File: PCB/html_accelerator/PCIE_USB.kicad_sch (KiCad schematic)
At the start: 19 parts, among them U1 MCS9990, U2 AP1513

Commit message: cap updates
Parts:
- C33: footprint Capacitor_SMD:C_0805_2012Metric_Pad1.18x1.45mm_HandSolder -> Capacitor_SMD:CP_Elec_10x10
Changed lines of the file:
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@@
       (effects (font (size 1.27 1.27)) (justify left))
     )
-    (property "Footprint" "Capacitor_SMD:C_0805_2012Metric_Pad1.18x1.45mm_HandSolder" (at 44.45 154.94 0)
+    (property "Footprint" "Capacitor_SMD:CP_Elec_10x10" (at 44.45 154.94 0)
       (effects (font (size 1.27 1.27)) hide)
     )
@@
       (effects (font (size 1.27 1.27)) (justify left))
     )
-    (property "Footprint" "Capacitor_SMD:C_0805_2012Metric_Pad1.18x1.45mm_HandSolder" (at 148.59 154.94 0)
-      (effects (font (size 1.27 1.27)) hide)
-    )
+    (property "Footprint" "Capacitor_SMD:CP_Elec_10x10" (at 148.59 154.94 0)
+      (effects (font (size 1.27 1.27)) hide)
+    )

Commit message: placement updates
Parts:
- added C33 (x2): 100uF, Capacitor_SMD:CP_Elec_6.3x5.8, symbol Device:C_Polarized_US
- C33: value 470uF -> 100uF; footprint Capacitor_SMD:CP_Elec_10x10 -> Capacitor_SMD:CP_Elec_6.3x5.8
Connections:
- net +12V: now also C33.1
- net GND: now also C33.2, C33.2
- net +3V3 renamed +5V
- net +5V: now also C33.1

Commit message: layout and 3d updates
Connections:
- net USB0_DM renamed 90_USB0_D_N
- net USB0_DP renamed 90_USB0_D_P
- net USB1_DM renamed 90_USB1_D_N
- net USB1_DP renamed 90_USB1_D_P
- net USB2_DM renamed 90_USB2_D_N
- net USB2_DP renamed 90_USB2_D_P
- net USB3_DM renamed 90_USB3_D_N
- net USB3_DP renamed 90_USB3_D_P
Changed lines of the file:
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@@
     (effects (font (size 1.27 1.27)) (justify left bottom))
   )
-  (global_label "USB1_DM" (shape bidirectional) (at 147.32 58.42 0) (fields_autoplaced)
+  (global_label "90_USB1_D_N" (shape bidirectional) (at 147.32 58.42 0) (fields_autoplaced)
     (effects (font (size 1.27 1.27)) (justify left))
-    (property "Intersheetrefs" "${INTERSHEET_REFS}" (at 160.0456 58.42 0)
+    (property "Intersheetrefs" "${INTERSHEET_REFS}" (at 164.2789 58.42 0)
       (effects (font (size 1.27 1.27)) (justify left))
     )
   )
-  (global_label "USB0_DM" (shape bidirectional) (at 147.32 43.18 0) (fields_autoplaced)
+  (global_label "90_USB0_D_N" (shape bidirectional) (at 147.32 43.18 0) (fields_autoplaced)
     (effects (font (size 1.27 1.27)) (justify left))
-    (property "Intersheetrefs" "${INTERSHEET_REFS}" (at 160.0456 43.18 0)
+    (property "Intersheetrefs" "${INTERSHEET_REFS}" (at 164.2789 43.18 0)
       (effects (font (size 1.27 1.27)) (justify left))
     )
   )
-  (global_label "USB3_DM" (shape bidirectional) (at 147.32 88.9 0) (fields_autoplaced)
+  (global_label "90_USB3_D_N" (shape bidirectional) (at 147.32 88.9 0) (fields_autoplaced)
     (effects (font (size 1.27 1.27)) (justify left))
-    (property "Intersheetrefs" "${INTERSHEET_REFS}" (at 160.0456 88.9 0)
+    (property "Intersheetrefs" "${INTERSHEET_REFS}" (at 164.2789 88.9 0)
       (effects (font (size 1.27 1.27)) (justify left))
     )
   )
-  (global_label "USB2_DM" (shape bidirectional) (at 147.32 73.66 0) (fields_autoplaced)
+  (global_label "90_USB2_D_N" (shape bidirectional) (at 147.32 73.66 0) (fields_autoplaced)
     (effects (font (size 1.27 1.27)) (justify left))
-    (property "Intersheetrefs" "${INTERSHEET_REFS}" (at 160.0456 73.66 0)
+    (property "Intersheetrefs" "${INTERSHEET_REFS}" (at 164.2789 73.66 0)
       (effects (font (size 1.27 1.27)) (justify left))
     )
   )
-  (global_label "USB3_DP" (shape bidirectional) (at 147.32 93.98 0) (fields_autoplaced)
+  (global_label "90_USB3_D_P" (shape bidirectional) (at 147.32 93.98 0) (fields_autoplaced)
     (effects (font (size 1.27 1.27)) (justify left))
-    (property "Intersheetrefs" "${INTERSHEET_REFS}" (at 159.8642 93.98 0)
+    (property "Intersheetrefs" "${INTERSHEET_REFS}" (at 164.2184 93.98 0)
       (effects (font (size 1.27 1.27)) (justify left))
     )
   )
-  (global_label "USB2_DP" (shape bidirectional) (at 147.32 78.74 0) (fields_autoplaced)
+  (global_label "90_USB2_D_P" (shape bidirectional) (at 147.32 78.74 0) (fields_autoplaced)
     (effects (font (size 1.27 1.27)) (justify left))
-    (property "Intersheetrefs" "${INTERSHEET_REFS}" (at 159.8642 78.74 0)
+    (property "Intersheetrefs" "${INTERSHEET_REFS}" (at 164.2184 78.74 0)
       (effects (font (size 1.27 1.27)) (justify left))
     )
   )
-  (global_label "USB0_DP" (shape bidirectional) (at 147.32 48.26 0) (fields_autoplaced)
+  (global_label "90_USB0_D_P" (shape bidirectional) (at 147.32 48.26 0) (fields_autoplaced)
     (effects (font (size 1.27 1.27)) (justify left))
-    (property "Intersheetrefs" "${INTERSHEET_REFS}" (at 159.8642 48.26 0)
+    (property "Intersheetrefs" "${INTERSHEET_REFS}" (at 164.2184 48.26 0)
       (effects (font (size 1.27 1.27)) (justify left))
     )
   )
-  (global_label "USB1_DP" (shape bidirectional) (at 147.32 63.5 0) (fields_autoplaced)
+  (global_label "90_USB1_D_P" (shape bidirectional) (at 147.32 63.5 0) (fields_autoplaced)
     (effects (font (size 1.27 1.27)) (justify left))
-    (property "Intersheetrefs" "${INTERSHEET_REFS}" (at 159.8642 63.5 0)
+    (property "Intersheetrefs" "${INTERSHEET_REFS}" (at 164.2184 63.5 0)
       (effects (font (size 1.27 1.27)) (justify left))
     )

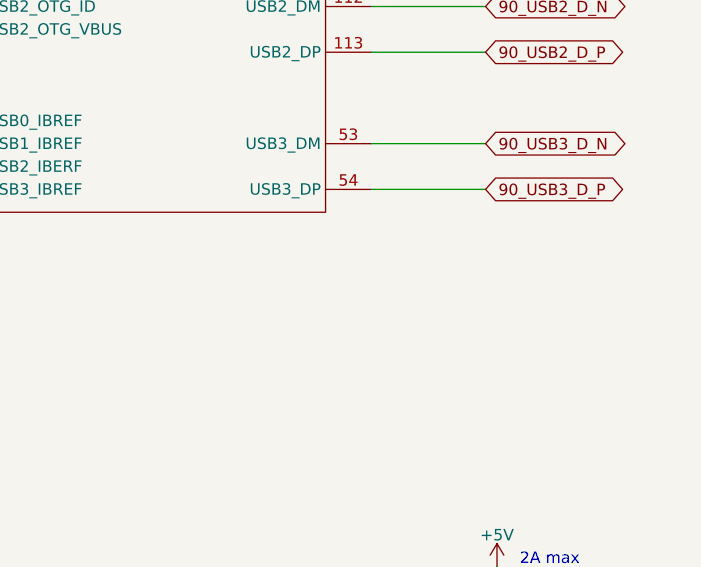
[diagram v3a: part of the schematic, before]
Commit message: impedance controlled nets
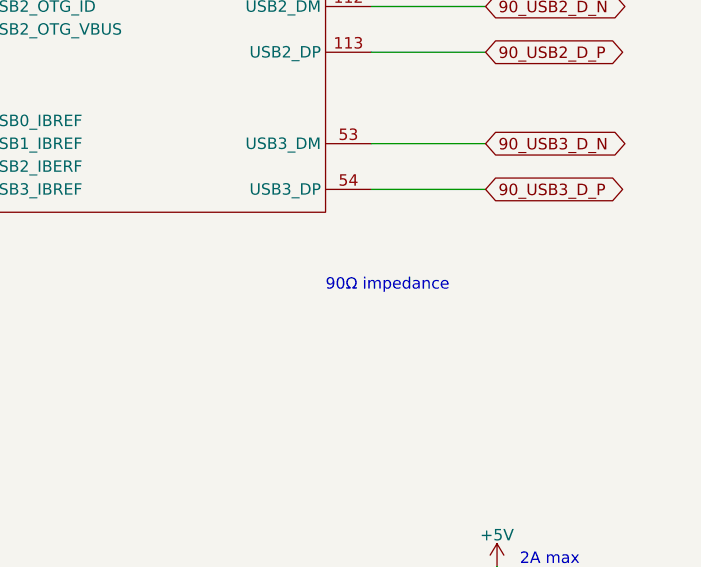
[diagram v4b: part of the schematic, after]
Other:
- note added: "90Ω impedance"
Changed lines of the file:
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@@
+    (effects (font (size 1.27 1.27)) (justify left bottom))
+  )
+  (text "90Ω impedance" (at 129.54 105.41 0)
     (effects (font (size 1.27 1.27)) (justify left bottom))
   )

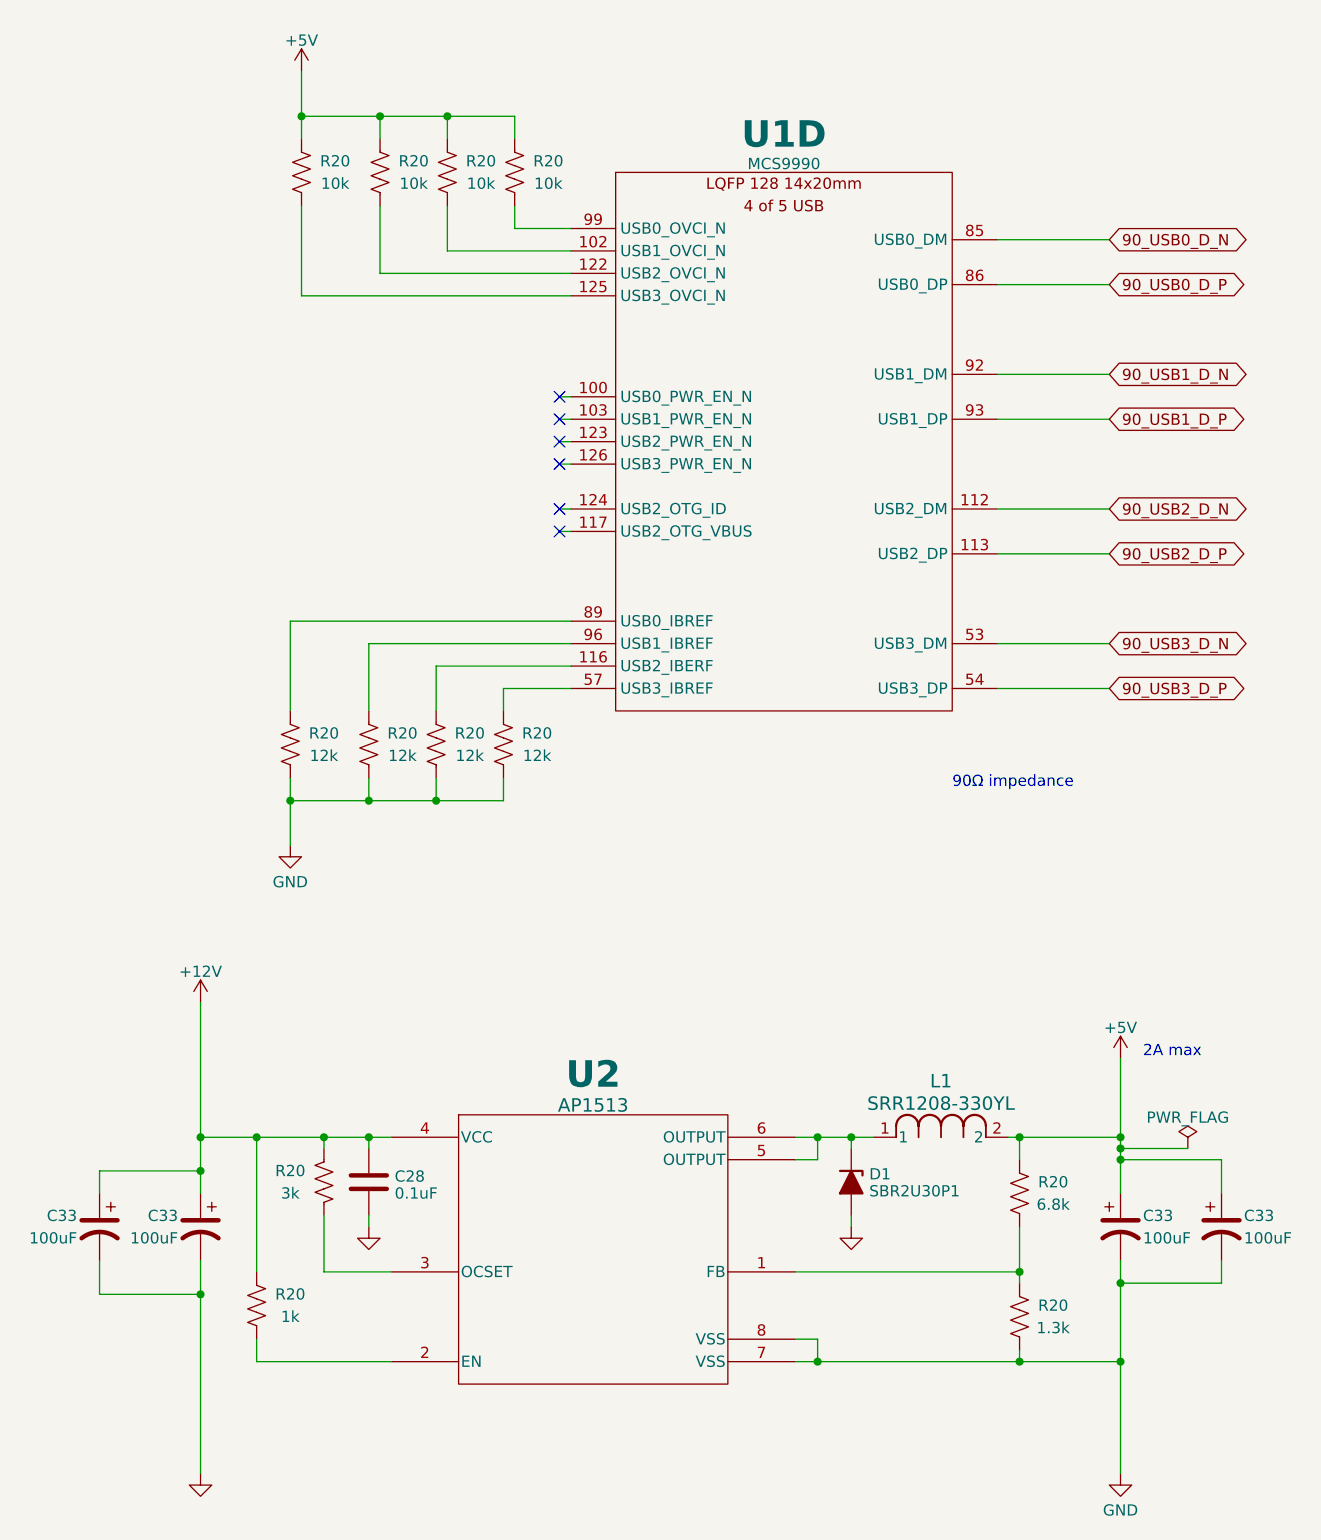
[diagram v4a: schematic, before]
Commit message: constraints for impedance control
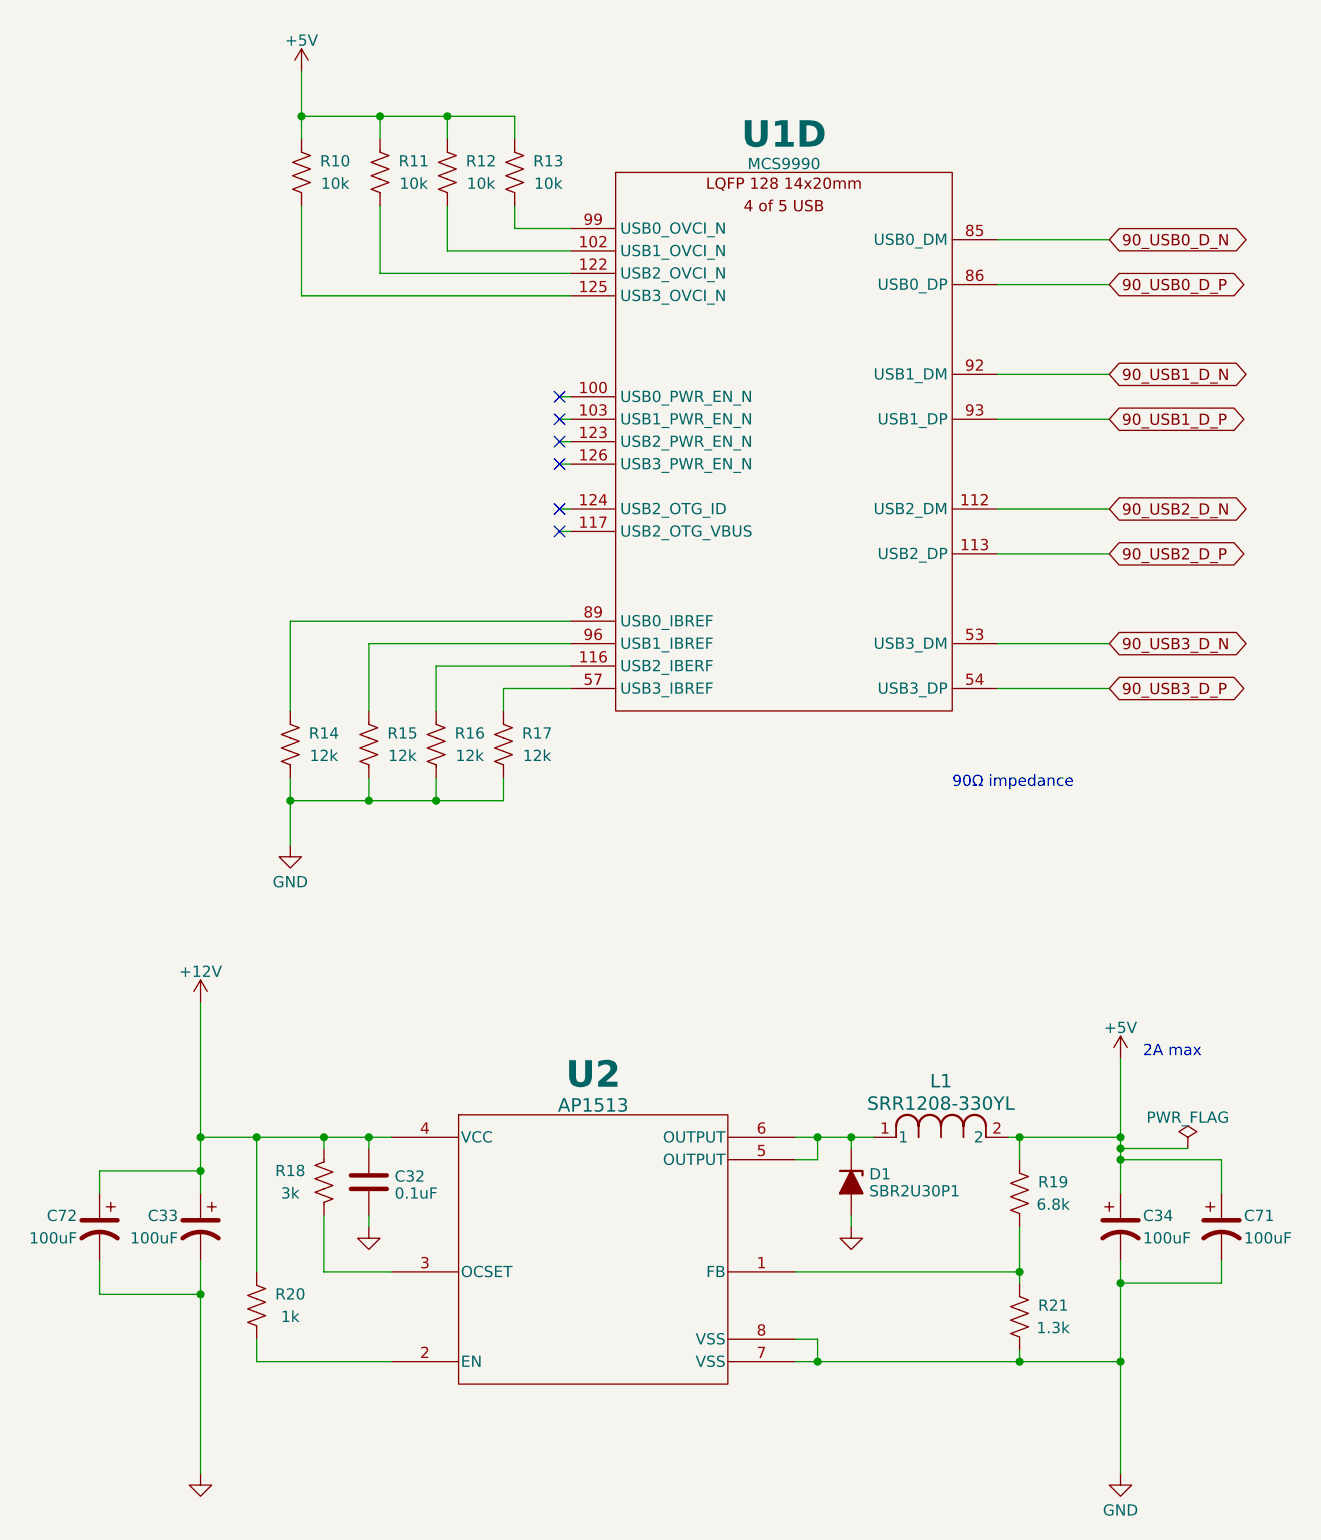
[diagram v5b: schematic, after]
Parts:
- renumbered C28 to C32, C33 to C34, C33 to C71, C33 to C72, R20 to R10, R20 to R11, R20 to R12, R20 to R13, R20 to R14, R20 to R15, R20 to R16, R20 to R17, R20 to R18, R20 to R19, R20 to R21

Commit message: gerbers and readme updates
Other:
- company: (none) -> Spencer K
- title: USB, 5v POWER -> HTML Accelerator
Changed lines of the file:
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@@
 	(paper "A4")
 	(title_block
-		(title "USB, 5v POWER")
-		(date "2024-09-15")
-		(rev "1")
+		(title "HTML Accelerator")
+		(date "2026-04-25")
+		(rev "1.0")
+		(company "Spencer K")
+		(comment 1 "https://github.com/akaStanley/HTML_Accelerator")
 	)
 	(text "2A max"
